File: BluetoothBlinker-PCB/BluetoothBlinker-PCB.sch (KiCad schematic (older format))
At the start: 51 parts, among them J1 USB_C_Receptacle_USB2.0, J2 Programming Connector, J3 Expansion Header, SW1 SW_Push, U1 CH340C, U2 TLV75533PDBV, U3 CC2642R, Y1 48MHz, Y2 32.768kHz

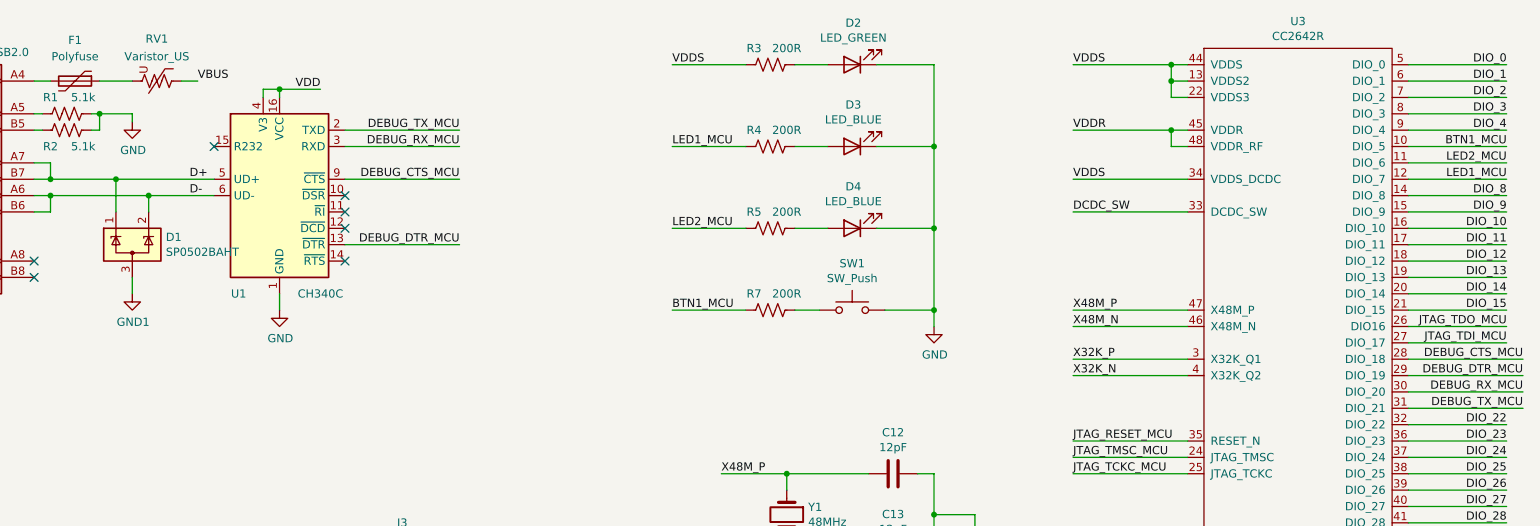
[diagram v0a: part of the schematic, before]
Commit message: Update to new USB Uart and generate PDF
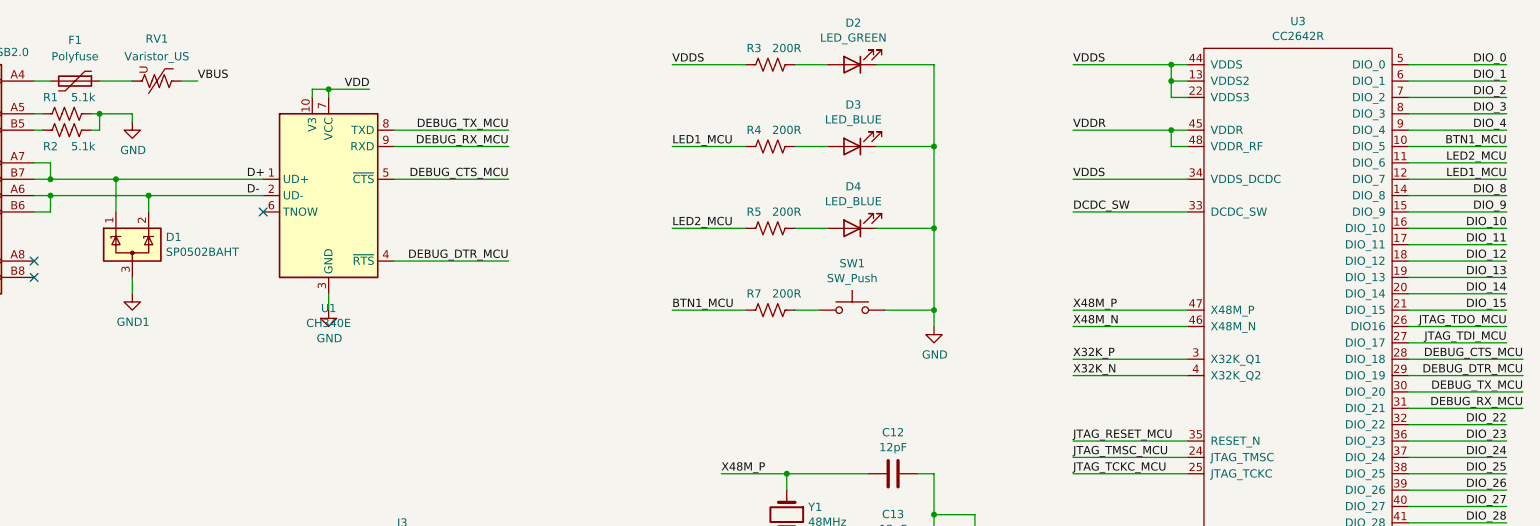
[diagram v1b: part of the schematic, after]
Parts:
- removed U1: CH340C, Package_SO:SOIC-16_3.9x9.9mm_P1.27mm, symbol Interface_USB:CH340C
- added U1: CH340E, Package_SO:MSOP-10_3x3mm_P0.5mm, symbol Interface_USB:CH340E
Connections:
- net D+: now also U1.1 (UD+)
- net D-: now also U1.2 (UD-)
- net DEBUG_CTS_MCU: now also U1.5 (~CTS)
- net DEBUG_DTR_MCU: now also U1.4 (~RTS)
- net DEBUG_RX_MCU: now also U3.31 (DIO_21), U1.9 (RXD); no longer U3.30 (DIO_20)
- net DEBUG_TX_MCU: now also U3.30 (DIO_20), U1.8 (TXD); no longer U3.31 (DIO_21)
- net GND: now also U1.3 (GND)
- net VDD: now also U1.10 (V3), U1.7 (VCC)
- no-connect marks 9 -> 5
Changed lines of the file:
@@
 	1400 2600 1400 2650
-Wire Wire Line
-	3100 1700 2500 1700
 Wire Wire Line
 	2000 1800 2100 1800
@@
 Wire Wire Line
 	2100 1700 2000 1700
-NoConn ~ 3900 1800
-NoConn ~ 3900 1900
-NoConn ~ 3900 2000
-NoConn ~ 3900 2200
-$Comp
-L Interface_USB:CH340C U1
-U 1 1 5FDFDF2C
-P 3500 1800
-F 0 "U1" H 3250 1200 50  0000 C CNN
-F 1 "CH340C" H 3750 1200 50  0000 C CNN
-F 2 "Package_SO:SOIC-16_3.9x9.9mm_P1.27mm" H 3550 1250 50  0001 L CNN
-F 3 "https://datasheet.lcsc.com/szlcsc/Jiangsu-Qin-Heng-CH340C_C84681.pdf" H 3150 2600 50  0001 C CNN
-	1    3500 1800
-	1    0    0    -1
-$EndComp
-Text Label 4600 1400 2    50   ~ 0
+Text Label 4900 1400 2    50   ~ 0
 DEBUG_TX_MCU
-Text Label 4600 1500 2    50   ~ 0
+Text Label 4900 1500 2    50   ~ 0
 DEBUG_RX_MCU
-Text Label 4600 1700 2    50   ~ 0
+Text Label 4900 1700 2    50   ~ 0
 DEBUG_CTS_MCU
-Text Label 4600 2100 2    50   ~ 0
-DEBUG_DTR_MCU
-Wire Wire Line
-	4600 1400 3900 1400
-Wire Wire Line
-	4600 1500 3900 1500
-Wire Wire Line
-	4600 1700 3900 1700
-Wire Wire Line
-	4600 2100 3900 2100
+Wire Wire Line
+	4900 1400 4200 1400
+Wire Wire Line
+	4900 1500 4200 1500
+Wire Wire Line
+	4900 1700 4200 1700
+Wire Wire Line
+	4900 2200 4200 2200
 $Comp
 L Regulator_Linear:TLV75533PDBV U2
@@
 	2700 1900 2700 1800
 Connection ~ 2700 1800
-Wire Wire Line
-	2700 1800 3100 1800
 $Comp
 L power:GND1 #PWR0105
@@
 Connection ~ 5950 7500
 Wire Wire Line
-	3500 1200 3500 1150
-Wire Wire Line
-	3500 1150 3400 1150
-Wire Wire Line
-	3400 1150 3400 1200
-Text Label 3750 1150 2    50   ~ 0
+	3800 1200 3800 1150
+Wire Wire Line
+	3800 1150 3700 1150
+Wire Wire Line
+	3700 1150 3700 1200
+Text Label 4050 1150 2    50   ~ 0
 VDD
 Wire Wire Line
-	3750 1150 3500 1150
-Connection ~ 3500 1150
-NoConn ~ 3100 1500
+	4050 1150 3800 1150
+Connection ~ 3800 1150
 $Comp
 L power:GND #PWR0106
 U 1 1 5FE7B169
-P 3500 2500
-F 0 "#PWR0106" H 3500 2250 50  0001 C CNN
-F 1 "GND" H 3505 2327 50  0000 C CNN
-F 2 "" H 3500 2500 50  0001 C CNN
-F 3 "" H 3500 2500 50  0001 C CNN
-	1    3500 2500
-	1    0    0    -1
-$EndComp
-Wire Wire Line
-	3500 2500 3500 2400
+P 3800 2500
+F 0 "#PWR0106" H 3800 2250 50  0001 C CNN
+F 1 "GND" H 3805 2327 50  0000 C CNN
+F 2 "" H 3800 2500 50  0001 C CNN
+F 3 "" H 3800 2500 50  0001 C CNN
+	1    3800 2500
+	1    0    0    -1
+$EndComp
+Wire Wire Line
+	3800 2500 3800 2400
 Text Label 11000 1000 2    50   ~ 0
 DIO_0
@@
 DEBUG_DTR_MCU
 Text Label 11100 3000 2    50   ~ 0
+DEBUG_TX_MCU
+Text Label 11100 3100 2    50   ~ 0
 DEBUG_RX_MCU
-Text Label 11100 3100 2    50   ~ 0
-DEBUG_TX_MCU
 Text Label 11000 3200 2    50   ~ 0
 DIO_22
@@
 Wire Wire Line
 	4000 4050 3500 4050
-Text Label 2950 1700 0    50   ~ 0
+Text Label 3300 1700 0    50   ~ 0
 D+
-Text Label 2950 1800 0    50   ~ 0
+Text Label 3300 1800 0    50   ~ 0
 D-
 $Comp
@@
 Text Label 11000 1500 2    50   ~ 0
 BTN1_MCU
+Text Label 4900 2200 2    50   ~ 0
+DEBUG_DTR_MCU
+NoConn ~ 3400 1900
+$Comp
+L Interface_USB:CH340E U1
+U 1 1 6081C6AF
+P 3800 1800
+F 0 "U1" H 3800 1111 50  0000 C CNN
+F 1 "CH340E" H 3800 1020 50  0000 C CNN
+F 2 "Package_SO:MSOP-10_3x3mm_P0.5mm" H 3850 1250 50  0001 L CNN
+F 3 "https://www.mpja.com/download/35227cpdata.pdf" H 3450 2600 50  0001 C CNN
+	1    3800 1800
+	1    0    0    -1
+$EndComp
+Wire Wire Line
+	2500 1700 3400 1700
+Wire Wire Line
+	2700 1800 3400 1800
 $EndSCHEMATC

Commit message: Minor updates
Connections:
- net GND: no longer D3.1 (K), D4.1 (K)
- net GND1: now also RV1.1
- net LED1_MCU: now also R4.2; no longer R4.1
- net LED2_MCU: now also R5.2; no longer R5.1
- net VBUS: now also F1.1, RV1.2; no longer RV1.1
- net VDDS: now also D3.2 (A), D4.2 (A)
- new net: D3.1 (K), R4.1
- new net: D4.1 (K), R5.1
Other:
- moved on the sheet: D3, D4, R4, R5, R7, RV1, SW1
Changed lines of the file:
@@
 Wire Wire Line
 	2600 2400 2600 2300
-$Comp
-L Device:Varistor_US RV1
-U 1 1 5FDD0C56
-P 2750 1100
-F 0 "RV1" V 2492 1100 50  0000 C CNN
-F 1 "Varistor_US" V 2600 1100 50  0000 C CNN
-F 2 "Resistor_SMD:R_0603_1608Metric" V 2680 1100 50  0001 C CNN
-F 3 "https://www.littelfuse.com/products/varistors/multilayer/mla/v5_5mla0603.aspx" H 2750 1100 50  0001 C CNN
-	1    2750 1100
-	0    1    1    0
-$EndComp
 Wire Wire Line
 	2100 1100 2000 1100
-Text Label 3000 1100 0    50   ~ 0
+Text Label 2950 750  0    50   ~ 0
 VBUS
-Wire Wire Line
-	3000 1100 2900 1100
-$Comp
-L Device:Polyfuse F1
-U 1 1 5FDFAF4B
-P 2250 1100
-F 0 "F1" V 2000 1100 50  0000 C CNN
-F 1 "Polyfuse" V 2100 1100 50  0000 C CNN
-F 2 "Resistor_SMD:R_1206_3216Metric" H 2300 900 50  0001 L CNN
-F 3 "https://www.littelfuse.com/~/media/electronics/datasheets/resettable_ptcs/littelfuse_ptc_low_rho_datasheet.pdf.pdf" H 2250 1100 50  0001 C CNN
-F 4 "1206L150SL" V 2250 1100 50  0001 C CNN "Device"
-	1    2250 1100
-	0    1    1    0
-$EndComp
 Wire Wire Line
 	2400 1100 2600 1100
@@
 L Device:LED D3
 U 1 1 60955642
-P 7000 1500
-F 0 "D3" H 6993 1245 50  0000 C CNN
-F 1 "LED_BLUE" H 6993 1336 50  0000 C CNN
-F 2 "LED_SMD:LED_0603_1608Metric" H 7000 1500 50  0001 C CNN
-F 3 "https://www.kingbrightusa.com/images/catalog/SPEC/APT3216QBC-D.pdf" H 7000 1500 50  0001 C CNN
-	1    7000 1500
+P 6500 2000
+F 0 "D3" H 6493 1745 50  0000 C CNN
+F 1 "LED_BLUE" H 6493 1836 50  0000 C CNN
+F 2 "LED_SMD:LED_0603_1608Metric" H 6500 2000 50  0001 C CNN
+F 3 "https://www.kingbrightusa.com/images/catalog/SPEC/APT3216QBC-D.pdf" H 6500 2000 50  0001 C CNN
+	1    6500 2000
 	-1   0    0    1
 $EndComp
@@
 L Device:R_US R4
 U 1 1 609814AB
-P 6500 1500
-F 0 "R4" V 6600 1600 50  0000 C CNN
-F 1 "200R" V 6600 1400 50  0000 C CNN
-F 2 "Resistor_SMD:R_0603_1608Metric" V 6540 1490 50  0001 C CNN
-F 3 "~" H 6500 1500 50  0001 C CNN
-	1    6500 1500
+P 7000 2000
+F 0 "R4" V 7100 2100 50  0000 C CNN
+F 1 "200R" V 7100 1900 50  0000 C CNN
+F 2 "Resistor_SMD:R_0603_1608Metric" V 7040 1990 50  0001 C CNN
+F 3 "~" H 7000 2000 50  0001 C CNN
+	1    7000 2000
 	0    -1   -1   0
 $EndComp
@@
 L Device:R_US R5
 U 1 1 60981A2C
-P 6500 2000
-F 0 "R5" V 6600 2100 50  0000 C CNN
-F 1 "200R" V 6600 1900 50  0000 C CNN
-F 2 "Resistor_SMD:R_0603_1608Metric" V 6540 1990 50  0001 C CNN
-F 3 "~" H 6500 2000 50  0001 C CNN
-	1    6500 2000
+P 7000 2500
+F 0 "R5" V 7100 2600 50  0000 C CNN
+F 1 "200R" V 7100 2400 50  0000 C CNN
+F 2 "Resistor_SMD:R_0603_1608Metric" V 7040 2490 50  0001 C CNN
+F 3 "~" H 7000 2500 50  0001 C CNN
+	1    7000 2500
 	0    -1   -1   0
 $EndComp
@@
 VDDS
 Wire Wire Line
+	6650 2500 6850 2500
+Wire Wire Line
 	6650 2000 6850 2000
-Wire Wire Line
-	6650 1500 6850 1500
 Wire Wire Line
 	6850 1000 6650 1000
@@
 L power:GND #PWR01
 U 1 1 6005E763
-P 7500 2600
-F 0 "#PWR01" H 7500 2350 50  0001 C CNN
-F 1 "GND" H 7505 2427 50  0000 C CNN
-F 2 "" H 7500 2600 50  0001 C CNN
-F 3 "" H 7500 2600 50  0001 C CNN
-	1    7500 2600
+P 7500 1600
+F 0 "#PWR01" H 7500 1350 50  0001 C CNN
+F 1 "GND" H 7505 1427 50  0000 C CNN
+F 2 "" H 7500 1600 50  0001 C CNN
+F 3 "" H 7500 1600 50  0001 C CNN
+	1    7500 1600
 	1    0    0    -1
 $EndComp
@@
 	7500 1000 7150 1000
 Wire Wire Line
-	7500 1000 7500 1500
-Connection ~ 7500 2000
-Wire Wire Line
-	7500 1500 7150 1500
-Connection ~ 7500 1500
-Wire Wire Line
-	7500 1500 7500 2000
-Text Label 5900 1500 0    50   ~ 0
+	7500 2000 7150 2000
+Text Label 7500 2000 0    50   ~ 0
 LED1_MCU
-Text Label 5900 2000 0    50   ~ 0
+Text Label 7500 2500 0    50   ~ 0
 LED2_MCU
 Wire Wire Line
-	5900 2000 6350 2000
-Wire Wire Line
-	5900 1500 6350 1500
+	5900 2000 6200 2000
 Wire Wire Line
 	5900 1000 6350 1000
@@
 $EndComp
 Wire Wire Line
-	7500 2000 7150 2000
+	7500 2500 7150 2500
 $Comp
 L Device:LED D4
 U 1 1 609562A4
-P 7000 2000
-F 0 "D4" H 6993 1745 50  0000 C CNN
-F 1 "LED_BLUE" H 6993 1836 50  0000 C CNN
-F 2 "LED_SMD:LED_0603_1608Metric" H 7000 2000 50  0001 C CNN
-F 3 "https://www.kingbrightusa.com/images/catalog/SPEC/APT3216QBC-D.pdf" H 7000 2000 50  0001 C CNN
-	1    7000 2000
+P 6500 2500
+F 0 "D4" H 6493 2245 50  0000 C CNN
+F 1 "LED_BLUE" H 6493 2336 50  0000 C CNN
+F 2 "LED_SMD:LED_0603_1608Metric" H 6500 2500 50  0001 C CNN
+F 3 "https://www.kingbrightusa.com/images/catalog/SPEC/APT3216QBC-D.pdf" H 6500 2500 50  0001 C CNN
+	1    6500 2500
 	-1   0    0    1
 $EndComp
 Wire Wire Line
-	7500 2000 7500 2500
-Wire Wire Line
-	7500 2500 7200 2500
-Connection ~ 7500 2500
-Wire Wire Line
-	7500 2500 7500 2600
-Text Label 5900 2500 0    50   ~ 0
+	7500 1500 7200 1500
+Text Label 5900 1500 0    50   ~ 0
 BTN1_MCU
 Wire Wire Line
-	5900 2500 6350 2500
+	5900 1500 6350 1500
 $Comp
 L Device:R_US R7
 U 1 1 6022C1CA
-P 6500 2500
-F 0 "R7" V 6600 2600 50  0000 C CNN
-F 1 "200R" V 6600 2400 50  0000 C CNN
-F 2 "Resistor_SMD:R_0603_1608Metric" V 6540 2490 50  0001 C CNN
-F 3 "~" H 6500 2500 50  0001 C CNN
-	1    6500 2500
+P 6500 1500
+F 0 "R7" V 6600 1600 50  0000 C CNN
+F 1 "200R" V 6600 1400 50  0000 C CNN
+F 2 "Resistor_SMD:R_0603_1608Metric" V 6540 1490 50  0001 C CNN
+F 3 "~" H 6500 1500 50  0001 C CNN
+	1    6500 1500
 	0    -1   -1   0
 $EndComp
 Wire Wire Line
-	6650 2500 6800 2500
+	6650 1500 6800 1500
 $Comp
 L BluetoothBlinker-PCB-rescue:Antenna-Device AE1
@@
 L Switch:SW_Push SW1
 U 1 1 601EE08E
-P 7000 2500
-F 0 "SW1" H 7000 2785 50  0000 C CNN
-F 1 "SW_Push" H 7000 2694 50  0000 C CNN
-F 2 "Button_Switch_THT:SW_PUSH_6mm" H 7000 2700 50  0001 C CNN
-F 3 "https://datasheet.octopart.com/TL3305AF160QG-E-Switch-datasheet-100437264.pdf" H 7000 2700 50  0001 C CNN
-	1    7000 2500
+P 7000 1500
+F 0 "SW1" H 7000 1785 50  0000 C CNN
+F 1 "SW_Push" H 7000 1694 50  0000 C CNN
+F 2 "Button_Switch_THT:SW_PUSH_6mm" H 7000 1700 50  0001 C CNN
+F 3 "https://datasheet.octopart.com/TL3305AF160QG-E-Switch-datasheet-100437264.pdf" H 7000 1700 50  0001 C CNN
+	1    7000 1500
 	1    0    0    -1
 $EndComp
@@
 Wire Wire Line
 	2700 1800 3400 1800
+Wire Wire Line
+	2600 750  2950 750
+Wire Wire Line
+	2600 750  2600 1100
+Wire Wire Line
+	2700 1100 2600 1100
+Connection ~ 2600 1100
+$Comp
+L power:GND1 #PWR0116
+U 1 1 60E8327C
+P 3100 1150
+F 0 "#PWR0116" H 3100 900 50  0001 C CNN
+F 1 "GND1" H 3105 977 50  0000 C CNN
+F 2 "" H 3100 1150 50  0001 C CNN
+F 3 "" H 3100 1150 50  0001 C CNN
+	1    3100 1150
+	1    0    0    -1
+$EndComp
+Wire Wire Line
+	3000 1100 3100 1100
+Wire Wire Line
+	3100 1100 3100 1150
+Wire Wire Line
+	7500 1000 7500 1500
+Wire Wire Line
+	7500 1600 7500 1500
+Connection ~ 7500 1500
+Wire Wire Line
+	6200 2500 6200 2000
+Wire Wire Line
+	6200 2500 6350 2500
+Connection ~ 6200 2000
+Wire Wire Line
+	6200 2000 6350 2000
+Text Label 5900 2000 0    50   ~ 0
+VDDS
+$Comp
+L Device:Varistor_US RV1
+U 1 1 5FDD0C56
+P 2850 1100
+F 0 "RV1" V 2592 1100 50  0000 C CNN
+F 1 "Varistor_US" V 2700 1100 50  0000 C CNN
+F 2 "Resistor_SMD:R_0603_1608Metric" V 2780 1100 50  0001 C CNN
+F 3 "https://www.littelfuse.com/products/varistors/multilayer/mla/v5_5mla0603.aspx" H 2850 1100 50  0001 C CNN
+	1    2850 1100
+	0    1    1    0
+$EndComp
+$Comp
+L Device:Polyfuse F1
+U 1 1 5FDFAF4B
+P 2250 1100
+F 0 "F1" V 2000 1100 50  0000 C CNN
+F 1 "Polyfuse" V 2100 1100 50  0000 C CNN
+F 2 "Resistor_SMD:R_1206_3216Metric" H 2300 900 50  0001 L CNN
+F 3 "https://www.littelfuse.com/~/media/electronics/datasheets/resettable_ptcs/littelfuse_ptc_low_rho_datasheet.pdf.pdf" H 2250 1100 50  0001 C CNN
+F 4 "1206L150SL" V 2250 1100 50  0001 C CNN "Device"
+	1    2250 1100
+	0    1    1    0
+$EndComp
 $EndSCHEMATC
